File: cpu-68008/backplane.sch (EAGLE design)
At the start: 45 parts, among them IC101 74HCT245, IC102 74HCT245, IC103 74HCT245, IC104 74HCT245, IC201 GAL22V10D

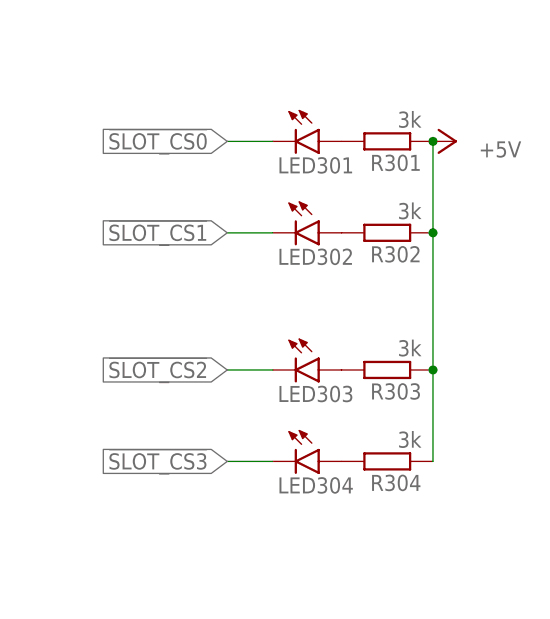
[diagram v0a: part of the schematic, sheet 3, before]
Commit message: minor revisions on mouser parts
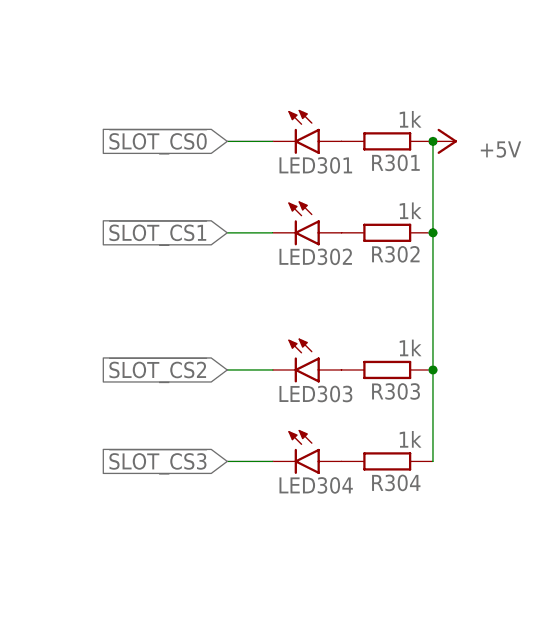
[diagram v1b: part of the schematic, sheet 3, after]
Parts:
- C102: value 47µF -> 220µF; device rcl:CPOL-EUE2-5 -> rcl:CPOL-EUE3.5-8; MOUSER 710-860020472006 -> 710-860020474012
- IC101, IC102, IC103, IC104: MOUSER (none) -> 595-SN74HCT245DBR
- IC201: MOUSER_SOCKET (none) -> 575-11044324
- R301, R302, R303, R304: value 3k -> 1k; MOUSER 652-CR0805JW-302ELF -> 652-CR0805FX-1001ELF
- SV301, SV302, SV303, SV304: MOUSER (none) -> 710-61304021821
